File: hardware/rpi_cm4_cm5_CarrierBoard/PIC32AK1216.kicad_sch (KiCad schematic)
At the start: 96 parts, among them J10 PR20206VBNN, Q21 2N7002, Q25 2N7002, Q26 2N7002, U1 PIC32AK1216GC41064-I/M7, U20 STWD100NYWY3F, Y3 20MHz

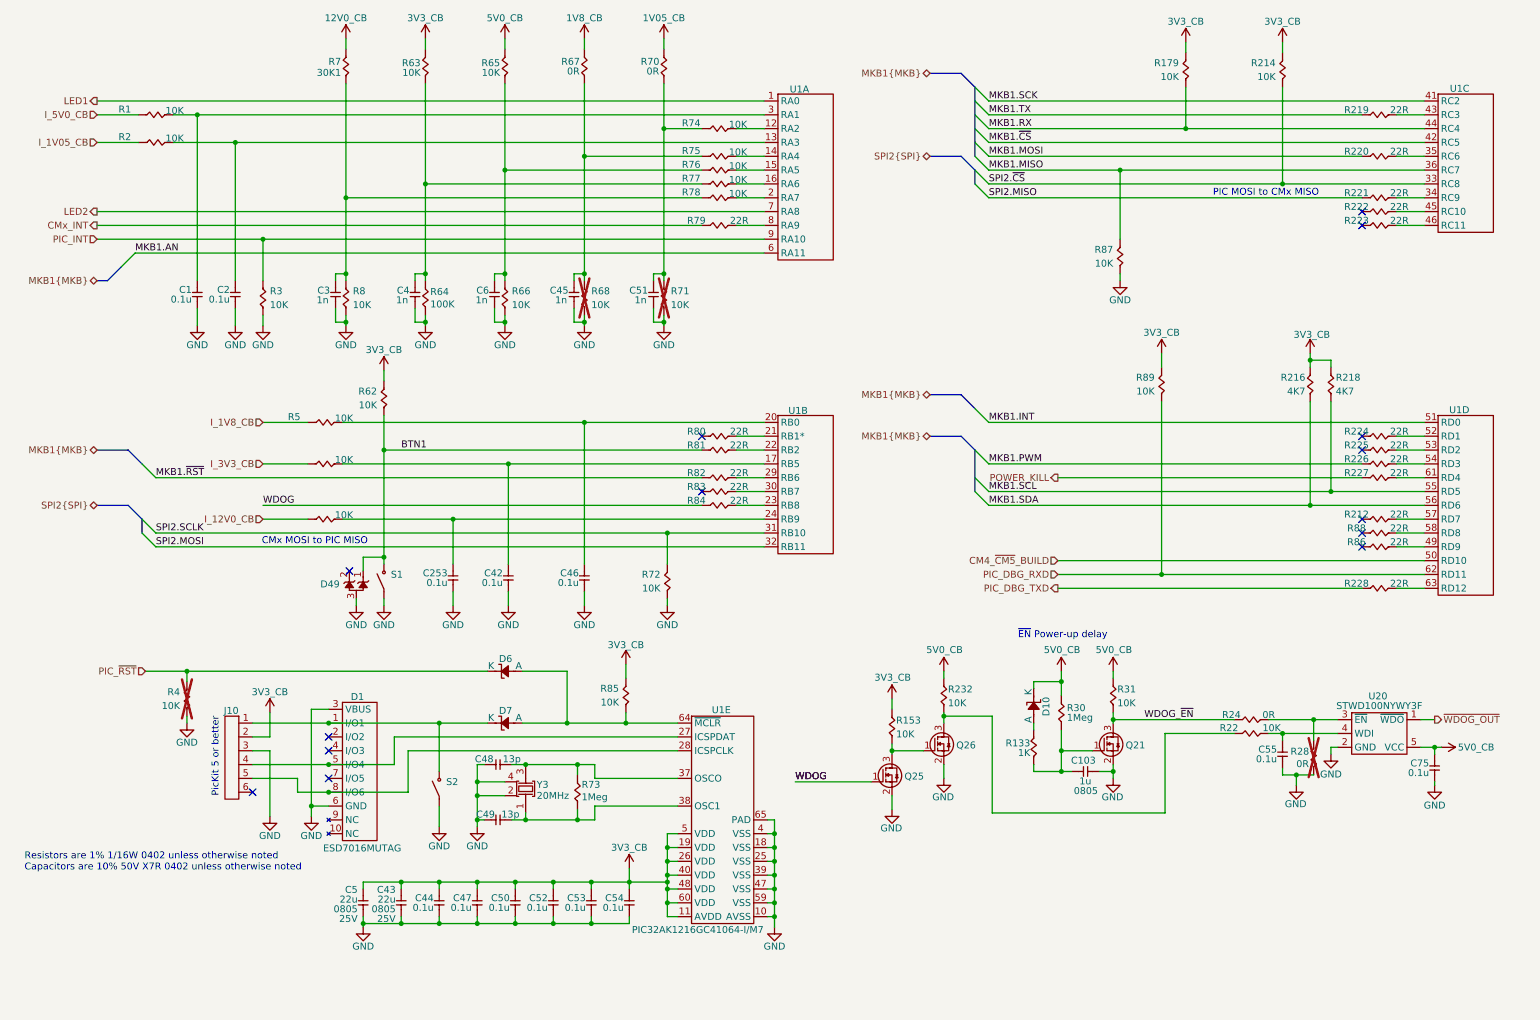
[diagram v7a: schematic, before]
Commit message: Document stackup Few changes to schematic based on preliminary PCB placement Update PinMux based on preliminary PCB placement and component positions
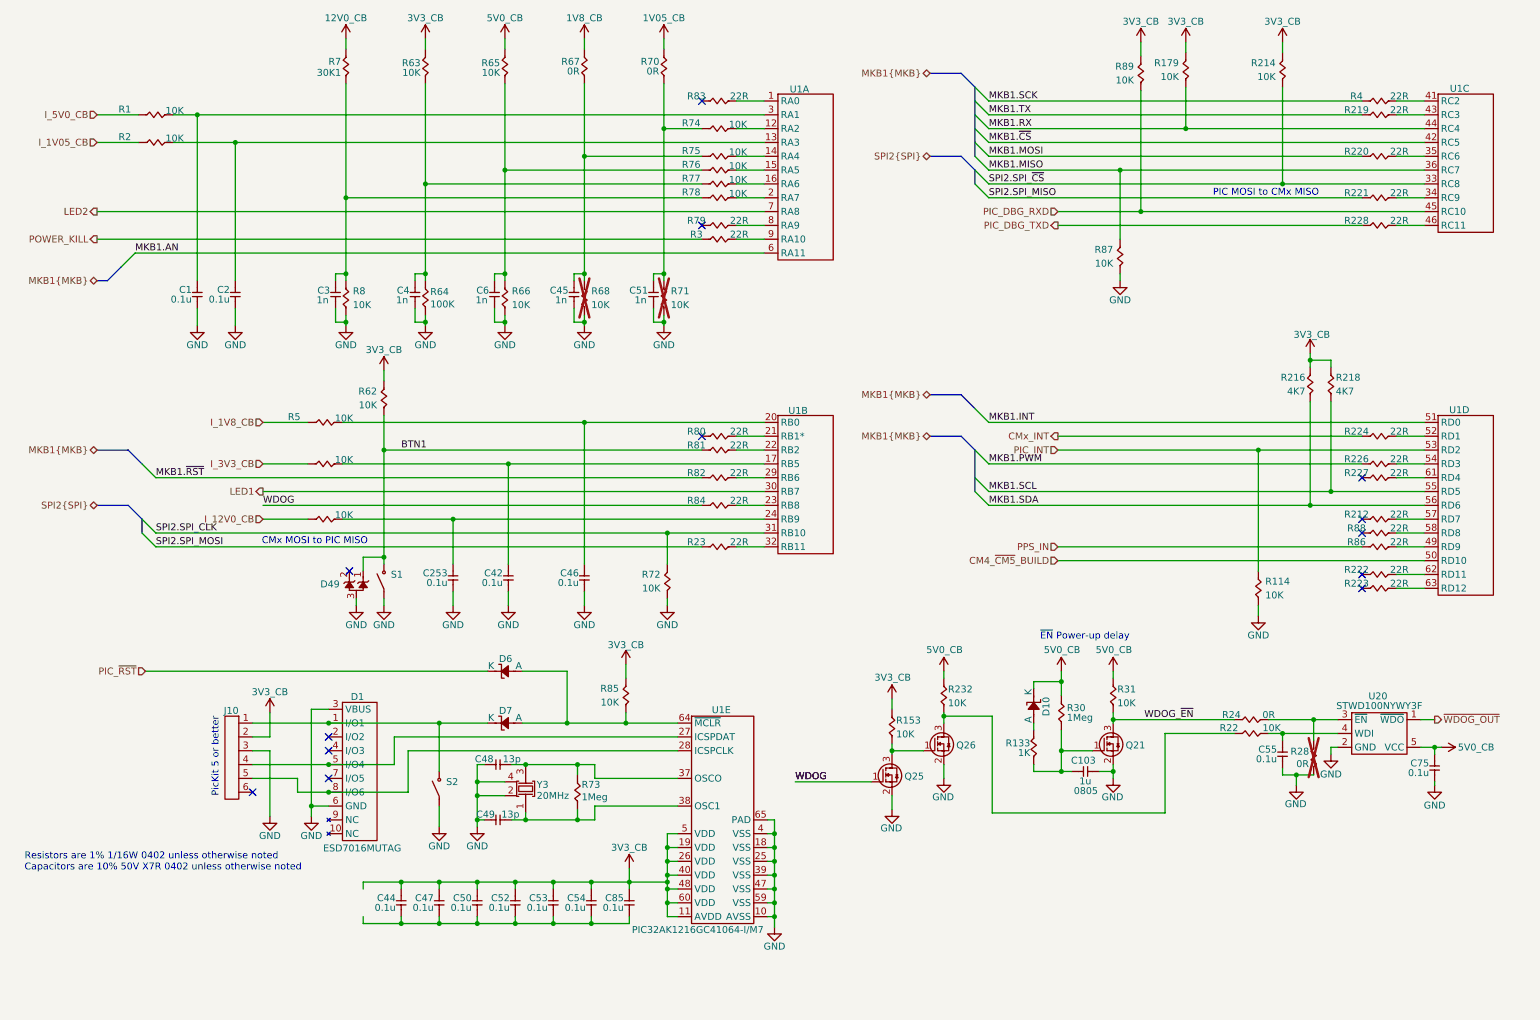
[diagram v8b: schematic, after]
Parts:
- removed C43, C5: 22u, footprint:CAP_NONPOL_0805, symbol KicadCompDb:Capacitors/CAP_CER_SMT_00011
- removed R225: 22R, footprint:RES_0402, symbol KicadCompDb:Resistors/RES_SMT_00015
- removed R3, R4: 10K, footprint:RES_0402, symbol KicadCompDb:Resistors/RES_SMT_00013
- added C85: 0.1u, footprint:CAP_NONPOL_0402, symbol KicadCompDb:Capacitors/CAP_CER_SMT_00001
- added R114: 10K, footprint:RES_0402, symbol KicadCompDb:Resistors/RES_SMT_00013
- added R23, R3, R4: 22R, footprint:RES_0402, symbol KicadCompDb:Resistors/RES_SMT_00015
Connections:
- net 3V3_CB: now also C85.2
- net CMx_INT: now also R224.2; no longer R79.2
- net GND: now also R114.1; no longer C44.1, C47.1, C50.1, C52.1, C53.1, C54.1
- net LED1: now also U1.30 (RB7); no longer U1.1 (RA0)
- net MKB1.SCK: now also R4.2; no longer U1.41 (RC2)
- net PIC_DBG_RXD: now also U1.45 (RC10); no longer U1.62 (RD11)
- net PIC_INT: now also U1.53 (RD2), R114.2; no longer U1.9 (RA10)
- net POWER_KILL: now also R3.2; no longer R227.2
- net at R222.1: now also U1.62 (RD11); no longer U1.45 (RC10)
- net at U1.46 (RC11): now also R228.1; no longer R223.1
- net at U1.63 (RD12): now also R223.1; no longer R228.1
- net at R83.1: now also U1.1 (RA0); no longer U1.30 (RB7)
- net PPS_IN: now reaches R86.2
- net SPI2.MISO renamed SPI2.SPI_MISO
- net SPI2.MOSI: no longer names the net of U1.32 (RB11)
- net SPI2.MOSI: now also R23.1
- net SPI2.SCLK renamed SPI2.SPI_CLK
- net SPI2.~{CS} renamed SPI2.SPI_~{CS}
- new net: C44.1, C47.1, C50.1, C52.1, C53.1, C54.1, C85.1
- new net: R4.1, U1.41 (RC2)
- new net: R3.1, U1.9 (RA10)
- new net SPI2.SPI_MOSI: R23.2
- no-connect marks 14 -> 13
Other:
- moved on the sheet: C44, C47, C50, C52, C53, C54, R222, R223, R228, R89
